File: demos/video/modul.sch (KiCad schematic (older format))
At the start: 39 parts, among them Q1 BC848, Q2 BC848, Q3 BC848, U20 TDA8501, X3 4,433618MH

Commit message: Pcbnew: Minor fix in hotkeys. Demos: add an example to use  a local fp-lib-table and local libs, and update schematics and boards.
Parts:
- C43, C44, C45, C46, C48, C53, C54, C58, C59, C60, C61, R10, R11, R16, R17, R18, R30, R31, R32, R33, R34, R39, R4, R40, R41, R9: footprint (none) -> lib_smd:SM1206
- C55, C64: footprint (none) -> lib_smd:SM1210L
- CV1: footprint (none) -> discret:CV3-30PF
- L1, L2, L3: footprint (none) -> lib_smd:SM1812
- L6: footprint (none) -> footprints:LRTDK
- POT1: footprint (none) -> lib_smd:POT_CMS
- Q1, Q2, Q3: footprint (none) -> lib_smd:SOT23EBC
- U20: footprint (none) -> lib_smd:SO24E
- X3: footprint (none) -> discret:HC-18UH

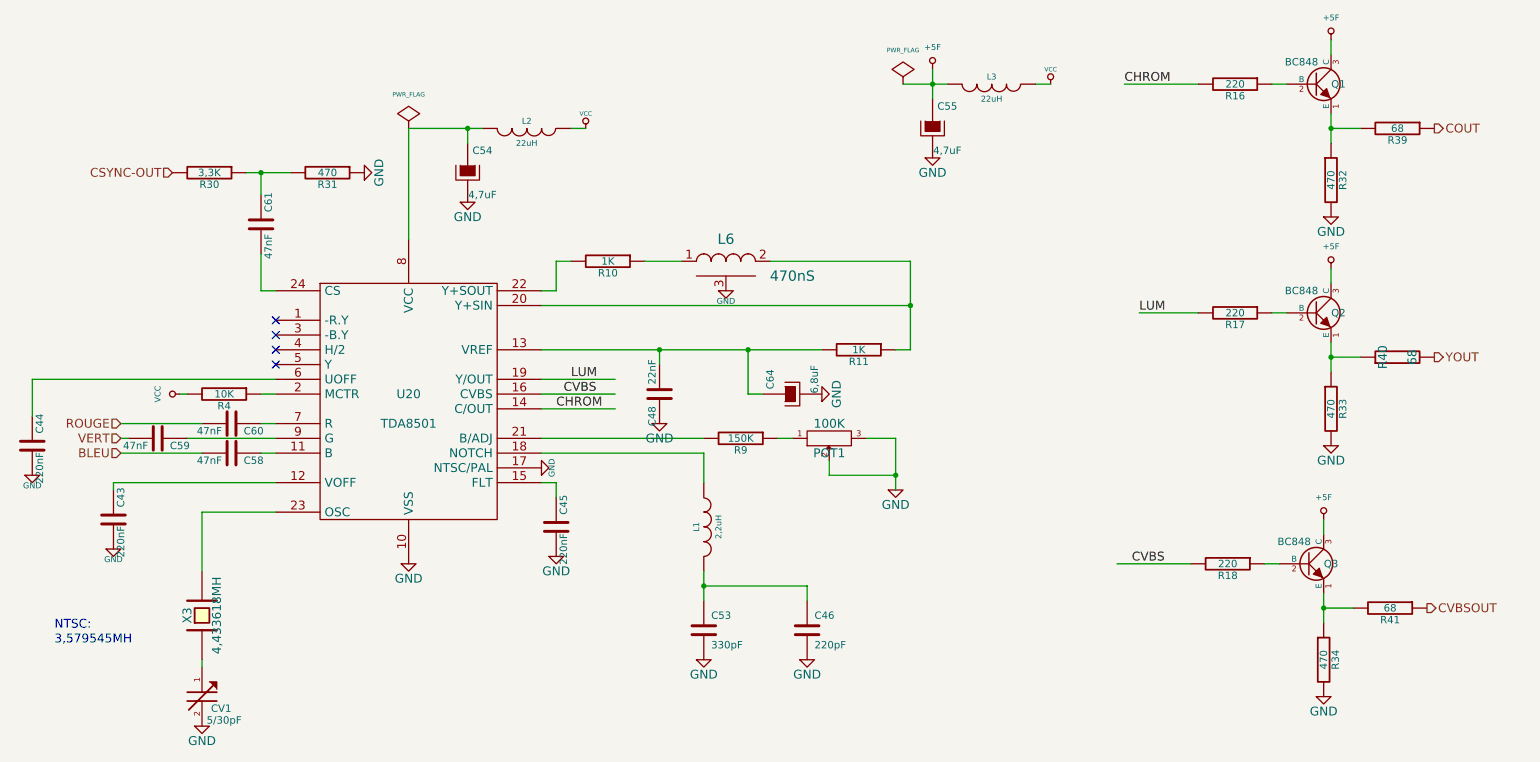
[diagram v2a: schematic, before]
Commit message: demos/ schematic tidying
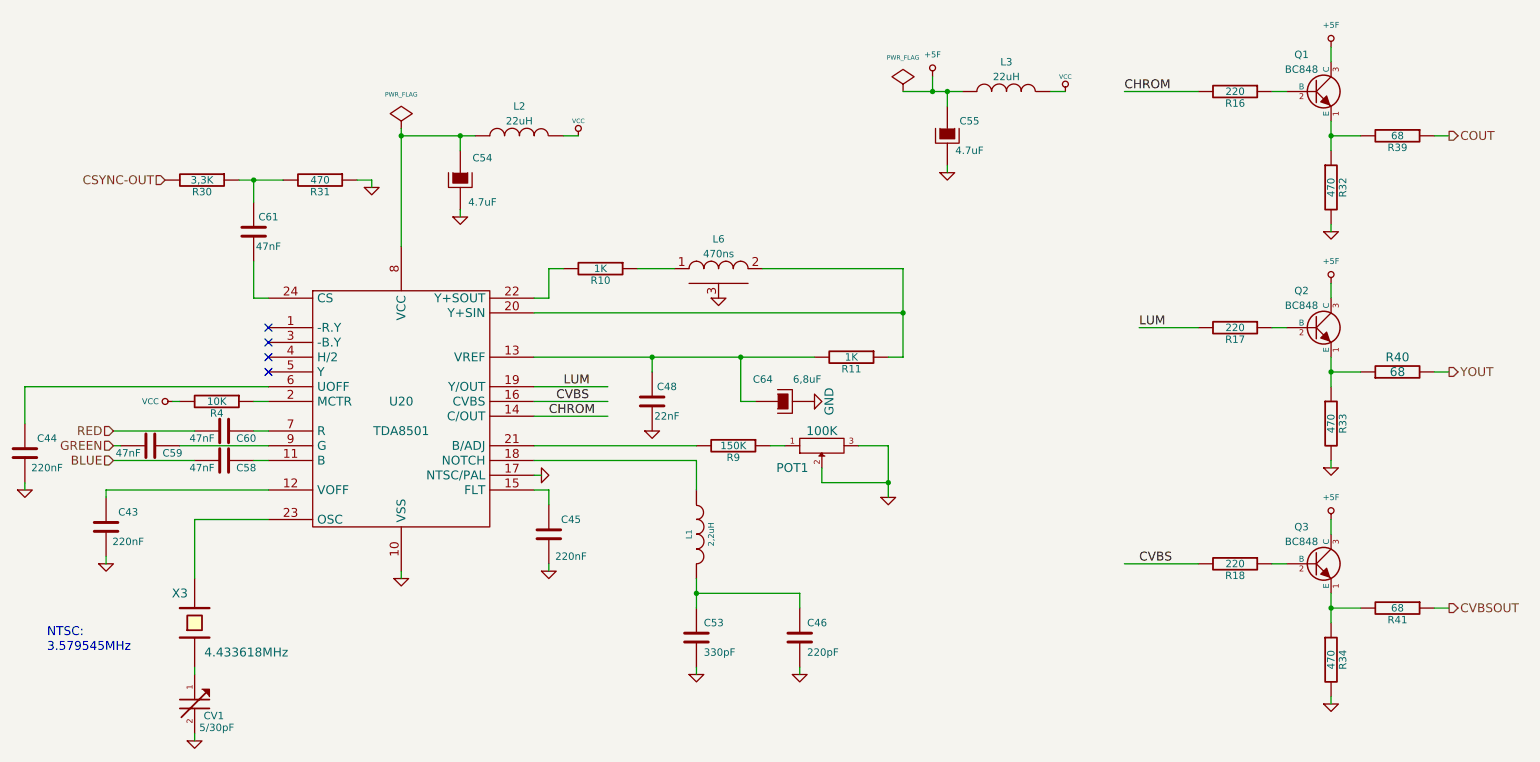
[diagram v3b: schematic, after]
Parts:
- C54, C55: value 4,7uF -> 4.7uF
- L6: value 470nS -> 470ns
- X3: value 4,433618MH -> 4.433618MHz
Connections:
- net labels added: BLUE, GREEN, RED
- net labels removed: BLEU, ROUGE, VERT
- wire segments 69 -> 88
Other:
- note added: "3.579545MHz"
- note removed: "3,579545MH"
- moved on the sheet: C43, C44, C45, C46, C48, C53, C54, C55, C58, C59, C60, C61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

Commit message: polygons in footprint body: fix incorrect calculation of polygons with clearance or outline thickness (fix bug #1511366) Clean demos
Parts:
- CV1: footprint discret:CV3-30PF -> Discret:CV3-30PF
- X3: footprint discret:HC-18UH -> Discret:HC-18UH
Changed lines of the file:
@@
 EESchema Schematic File Version 2
+LIBS:video_schlib
 LIBS:power
-LIBS:device
-LIBS:transistors
-LIBS:conn
-LIBS:linear
-LIBS:regul
-LIBS:74xx
-LIBS:cmos4000
-LIBS:adc-dac
-LIBS:memory
-LIBS:xilinx
-LIBS:special
-LIBS:analog_switches
-LIBS:motorola
-LIBS:intel
-LIBS:audio
-LIBS:interface
-LIBS:philips
-LIBS:cypress
-LIBS:siliconi
 LIBS:video-cache
 EELAYER 25 0
@@
 F 0 "CV1" H 2230 5270 50  0000 C CNN
 F 1 "5/30pF" H 2250 5190 50  0000 C CNN
-F 2 "discret:CV3-30PF" H 2100 5350 60  0001 C CNN
+F 2 "Discret:CV3-30PF" H 2100 5350 60  0001 C CNN
 F 3 "" H 2100 5350 60  0001 C CNN
 	1    2100 5350
@@
 F 0 "X3" V 2300 4900 60  0000 C CNN
 F 1 "4.433618MHz" V 1900 4450 60  0000 C CNN
-F 2 "discret:HC-18UH" H 2100 4800 60  0001 C CNN
+F 2 "Discret:HC-18UH" H 2100 4800 60  0001 C CNN
 F 3 "" H 2100 4800 60  0001 C CNN
 	1    2100 4800
